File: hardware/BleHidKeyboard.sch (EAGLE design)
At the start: 13 parts, among them IC1 MCP23018SO, IC2 MCP23018SO, J1 BATTERY, J4 KEYBOARD_2X13, U1 DYNASTREAM_N5150M5CD

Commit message: Version 1 of PCB layout
This is the version that I sent to OSHPark to have manufactured on
3/14/2018.
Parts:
- removed J2: (no value), SparkFun-Connectors:M041X04_NO_SILK
- removed J3: (no value), SparkFun-Connectors:M01NOSILK-KIT
- added JP1: DEBUG, adam_custom:FTSH-105
- added JP2: FTDI, adafruit:PINHD-1X6CLEAN
- IC1, IC2: value MCP23018SO -> MCP23018SSOP; device adam_custom:MCP23018SO -> adam_custom:MCP23018SSOP
- renumbered LED1 to LED_NUM, LED2 to LED_CAPS, LED3 to LED_CONNECT
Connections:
- removed net INT: J3.1, U1.P3
- new net !RST/!SWDIO: JP1.2, U1.!RST!/SWDIO
- new net SWDCLK: JP1.4, U1.SWDCLK
- new net UART_RXD: JP2.4, U1.P12
- new net UART_TXD: JP2.5, U1.P6
- net GND: now also JP1.3, JP1.5, JP1.9, JP2.1, JP2.2
- net INTA-1: now also U1.P3; no longer J2.1
- net INTA-2: now also U1.P11; no longer J2.3
- net INTB-1: now also U1.P8; no longer J2.2
- net INTB-2: now also U1.P21; no longer J2.4
- net KEY1: now also IC1.GPB7; no longer IC1.GPA0
- net KEY10: now also IC1.GPA6; no longer IC1.GPB1
- net KEY11: now also IC1.GPA5; no longer IC1.GPB2
- net KEY12: now also IC1.GPA4; no longer IC1.GPB3
- net KEY13: now also IC1.GPA3; no longer IC1.GPB4
- net KEY14: now also IC1.GPA2; no longer IC1.GPB5
- net KEY15: now also IC1.GPA1; no longer IC1.GPB6
- net KEY16: now also IC1.GPA0; no longer IC1.GPB7
- net KEY17: now also IC2.GPB1; no longer IC2.GPA0
- net KEY18: now also IC2.GPB0; no longer IC2.GPA1
- net KEY19: now also IC2.GPA7; no longer IC2.GPA2
- net KEY2: now also IC1.GPB6; no longer IC1.GPA1
- net KEY20: now also IC2.GPA6; no longer IC2.GPA3
- net KEY21: now also IC2.GPA5; no longer IC2.GPA4
- net KEY22: now also IC2.GPA4; no longer IC2.GPA5
- net KEY23: now also IC2.GPA3; no longer IC2.GPA6
- net KEY24: now also IC2.GPA2; no longer IC2.GPA7
- net KEY25: now also IC2.GPA1; no longer IC2.GPB0
- net KEY26: now also IC2.GPA0; no longer IC2.GPB1
- net KEY3: now also IC1.GPB5; no longer IC1.GPA2
- net KEY4: now also IC1.GPB4; no longer IC1.GPA3
- net KEY5: now also IC1.GPB3; no longer IC1.GPA4
- net KEY6: now also IC1.GPB2; no longer IC1.GPA5
- net KEY7: now also IC1.GPB1; no longer IC1.GPA6
- net KEY8: now also IC1.GPB0; no longer IC1.GPA7
- net KEY9: now also IC1.GPA7; no longer IC1.GPB0
- net LED_CAPS: now also U1.P0; no longer U1.P5
- net LED_CONNECT: now also U1.P9; no longer U1.P6
- net LED_NUM: now also U1.P24; no longer U1.P4
- net SCL: now also U1.P15; no longer U1.P1
- net SDA: now also U1.P5; no longer U1.P2
- net VCC: now also JP1.1
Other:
- moved on the sheet: IC1, IC2, U1

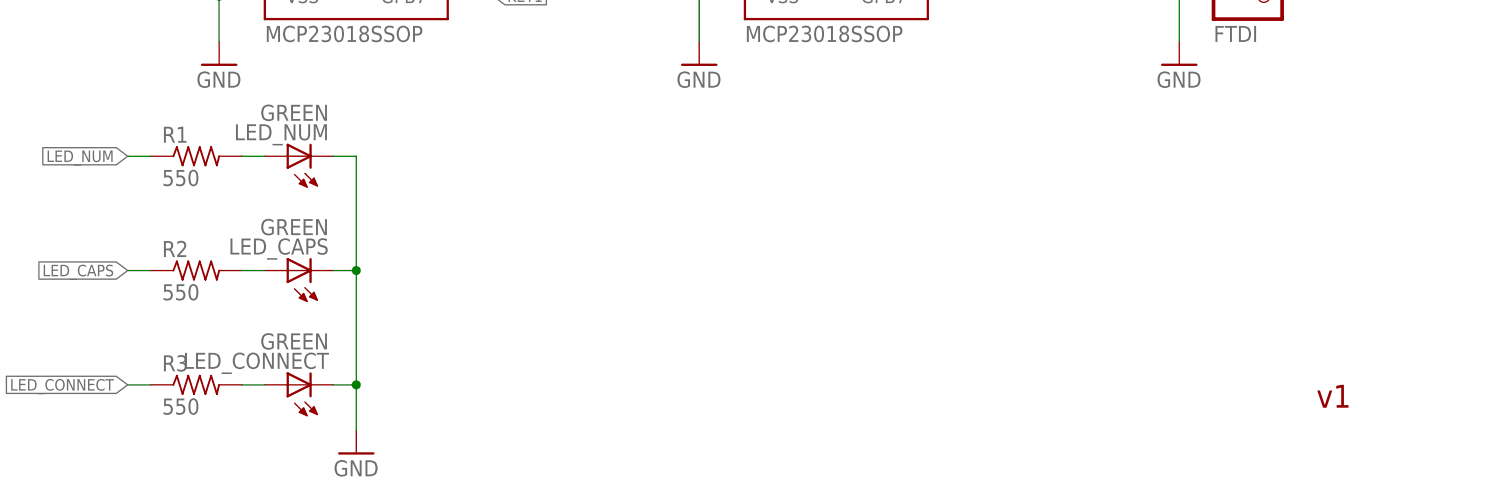
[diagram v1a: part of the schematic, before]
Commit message: Switch to 1.2k LED current limiting resistors
This reduces current usage by half but still leaves them bright enough
to see.
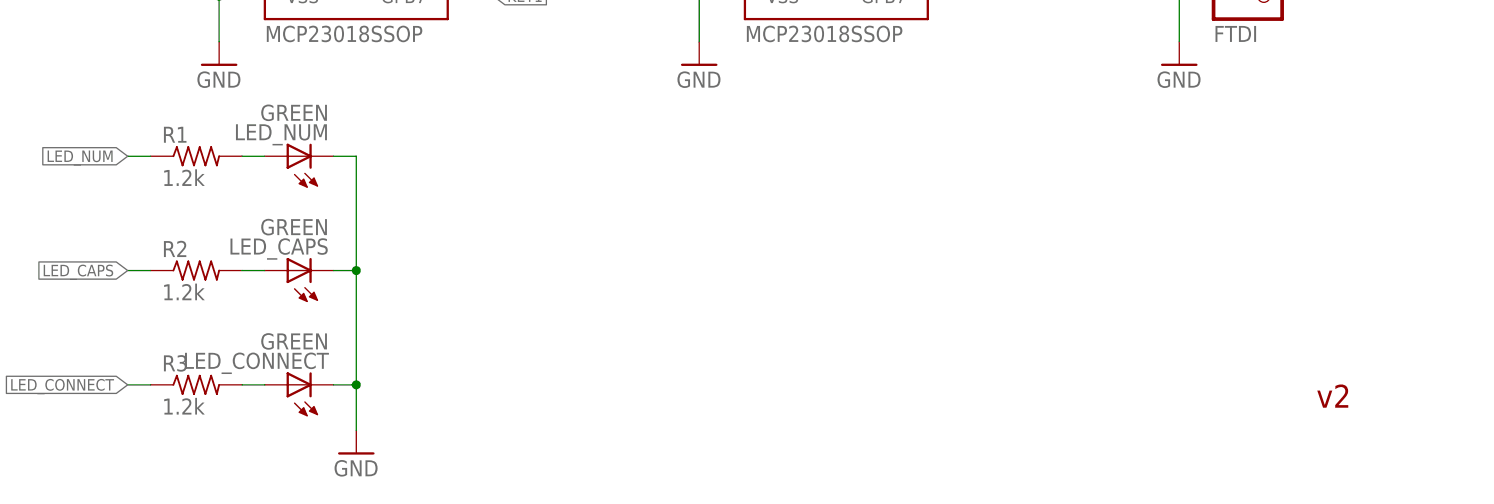
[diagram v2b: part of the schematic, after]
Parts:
- R1, R2, R3: value 550 -> 1.2k
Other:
- note added: "v2"
- note removed: "v1"
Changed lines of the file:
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@@
 <part name="GND4" library="SparkFun-Aesthetics" deviceset="GND" device=""/>
 <part name="J4" library="adam_custom" deviceset="KEYBOARD_2X13" device=""/>
-<part name="R1" library="rcl" deviceset="R-US_" device="R0805" value="550"/>
+<part name="R1" library="rcl" deviceset="R-US_" device="R0805" value="1.2k"/>
 <part name="LED_NUM" library="adafruit" deviceset="LED" device="CHIPLED_1206" value="GREEN"/>
-<part name="R2" library="rcl" deviceset="R-US_" device="R0805" value="550"/>
+<part name="R2" library="rcl" deviceset="R-US_" device="R0805" value="1.2k"/>
 <part name="LED_CAPS" library="adafruit" deviceset="LED" device="CHIPLED_1206" value="GREEN"/>
-<part name="R3" library="rcl" deviceset="R-US_" device="R0805" value="550"/>
+<part name="R3" library="rcl" deviceset="R-US_" device="R0805" value="1.2k"/>
 <part name="LED_CONNECT" library="adafruit" deviceset="LED" device="CHIPLED_1206" value="GREEN"/>
 <part name="GND5" library="SparkFun-Aesthetics" deviceset="GND" device=""/>
@@
 <sheet>
 <plain>
-<text x="233.68" y="10.16" size="2.54" layer="94">v1</text>
+<text x="233.68" y="10.16" size="2.54" layer="94">v2</text>
 </plain>
 <instances>

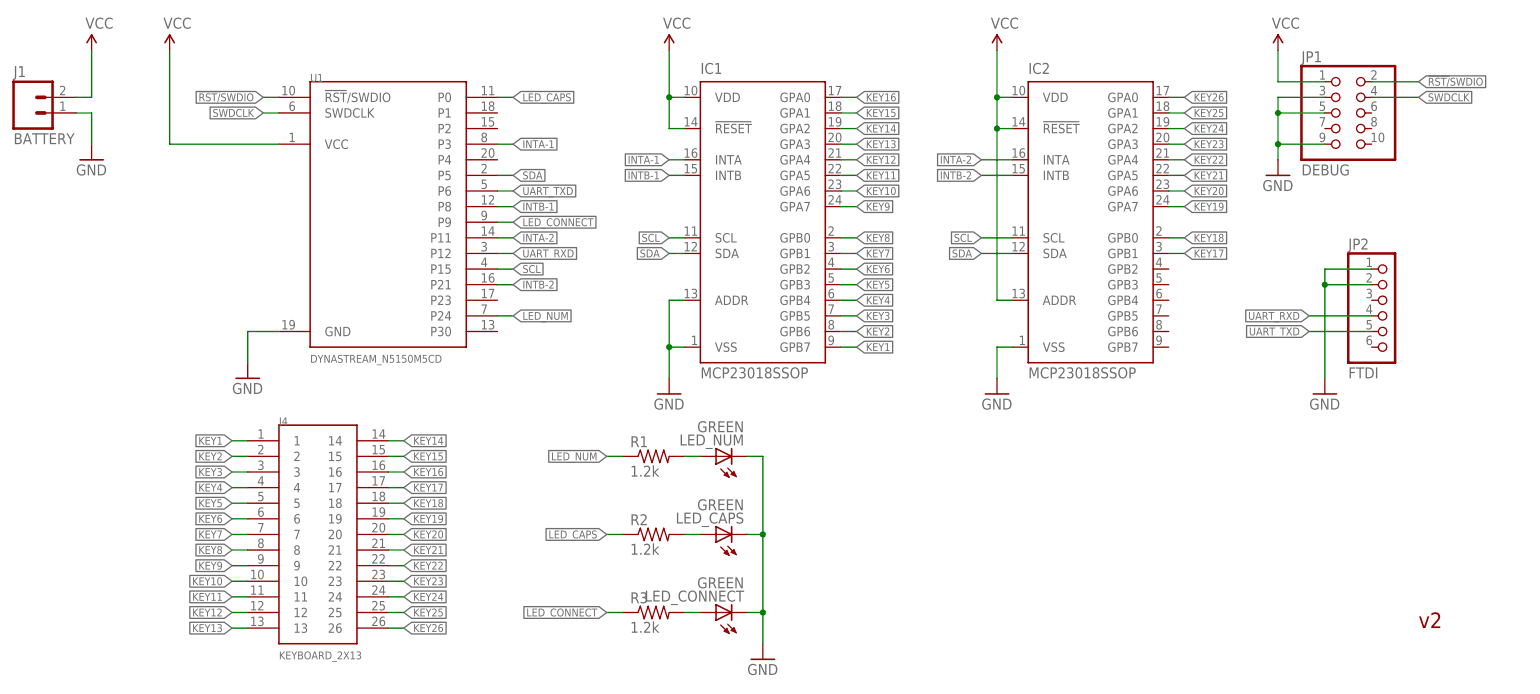
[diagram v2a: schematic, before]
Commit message: Version 3 of the PCB design
This is the design being sent off to OSHPark on May 6th, 2018.

This version of the PCB no longer uses the 20-pin Molex connector on
the bottom of the Dynastream N5150M5CD module and instead uses the
pads around the perimeter of the N5150M4CD module (actually the same
module but without the Molex and SWD connectors) instead. The module
will now mount on the bottom of the PCB with the module can sticking up
through a hole in this new PCB. This will give us extra height
clearance and correct the problem that the current PCB doesn't fit in
the original keyboard case.

I updated the firmware to accomodate the change in pin mappings for
UART, I2C, LEDs, etc.
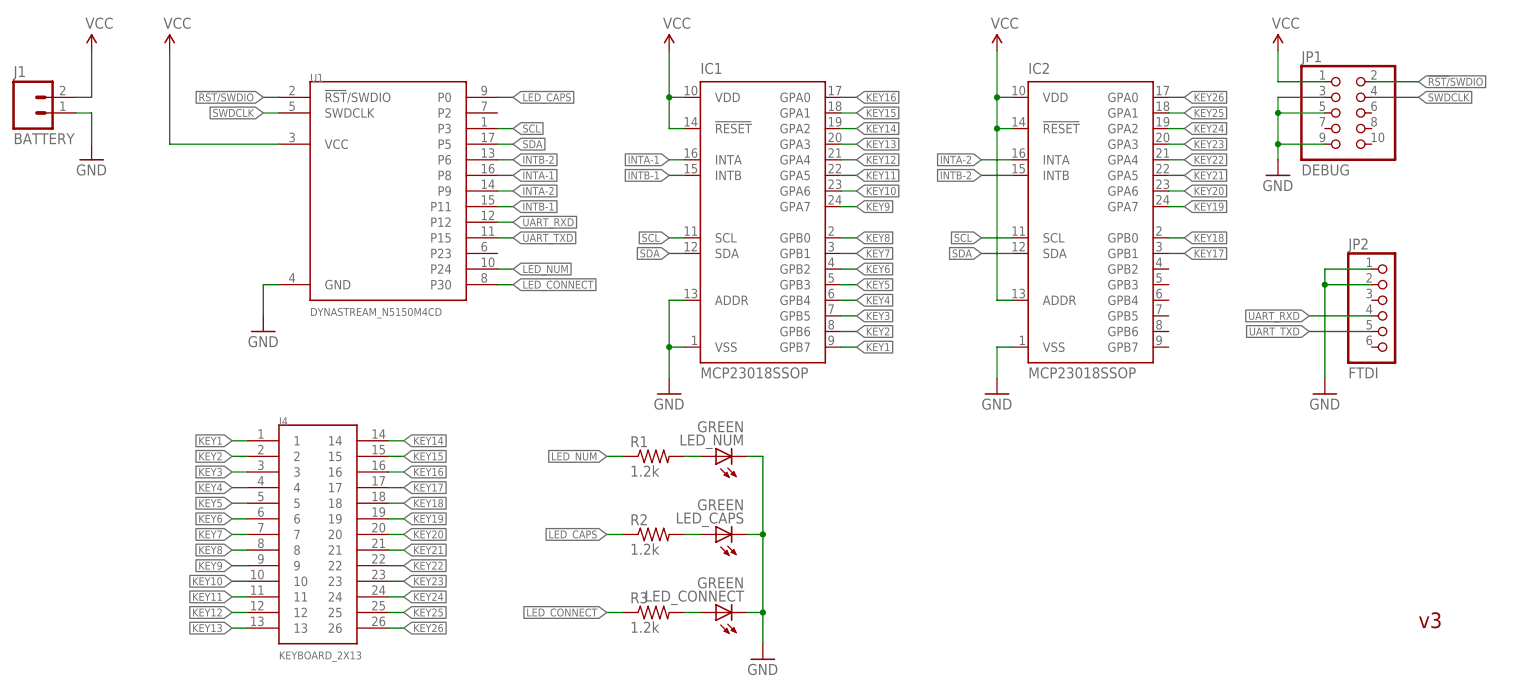
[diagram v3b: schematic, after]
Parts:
- U1: value DYNASTREAM_N5150M5CD -> DYNASTREAM_N5150M4CD; device adam_custom:DYNASTREAM_N5150M5CD -> adam_custom:DYNASTREAM_N5150M4CD
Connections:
- net INTA-1: now also U1.P8; no longer U1.P3
- net INTA-2: now also U1.P9; no longer U1.P11
- net INTB-1: now also U1.P11; no longer U1.P8
- net INTB-2: now also U1.P6; no longer U1.P21
- net LED_CONNECT: now also U1.P30; no longer U1.P9
- net SCL: now also U1.P3; no longer U1.P15
- net UART_TXD: now also U1.P15; no longer U1.P6
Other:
- note added: "v3"
- note removed: "v2"
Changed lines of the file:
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@@
 <part name="SUPPLY1" library="SparkFun-Aesthetics" deviceset="VCC" device=""/>
 <part name="GND1" library="SparkFun-Aesthetics" deviceset="GND" device=""/>
-<part name="U1" library="adam_custom" deviceset="DYNASTREAM_N5150M5CD" device=""/>
+<part name="U1" library="adam_custom" deviceset="DYNASTREAM_N5150M4CD" device=""/>
 <part name="SUPPLY2" library="SparkFun-Aesthetics" deviceset="VCC" device=""/>
 <part name="GND2" library="SparkFun-Aesthetics" deviceset="GND" device=""/>
@@
 <sheet>
 <plain>
-<text x="233.68" y="10.16" size="2.54" layer="94">v2</text>
+<text x="233.68" y="10.16" size="2.54" layer="94">v3</text>
 </plain>
 <instances>
@@
 <instance part="U1" gate="G$1" x="66.04" y="78.74"/>
 <instance part="SUPPLY2" gate="G$1" x="30.48" y="104.14"/>
-<instance part="GND2" gate="1" x="43.18" y="50.8"/>
+<instance part="GND2" gate="1" x="45.72" y="58.42"/>
 <instance part="IC1" gate="G$1" x="127" y="76.2"/>
 <instance part="SUPPLY3" gate="G$1" x="111.76" y="104.14"/>
@@
 </segment>
 <segment>
-<pinref part="U1" gate="G$1" pin="GND"/>
-<pinref part="GND2" gate="1" pin="GND"/>
-<wire x1="48.26" y1="58.42" x2="43.18" y2="58.42" width="0.1524" layer="91"/>
-<wire x1="43.18" y1="58.42" x2="43.18" y2="53.34" width="0.1524" layer="91"/>
-</segment>
-<segment>
 <pinref part="IC1" gate="G$1" pin="VSS"/>
 <pinref part="GND3" gate="1" pin="GND"/>
@@
 <junction x="218.44" y="66.04"/>
 </segment>
+<segment>
+<pinref part="U1" gate="G$1" pin="GND"/>
+<pinref part="GND2" gate="1" pin="GND"/>
+<wire x1="48.26" y1="66.04" x2="45.72" y2="66.04" width="0.1524" layer="91"/>
+<wire x1="45.72" y1="66.04" x2="45.72" y2="60.96" width="0.1524" layer="91"/>
+</segment>
 </net>
 <net name="SCL" class="0">
@@
 </segment>
 <segment>
-<pinref part="U1" gate="G$1" pin="P15"/>
-<wire x1="83.82" y1="68.58" x2="86.36" y2="68.58" width="0.1524" layer="91"/>
-<label x="86.36" y="68.58" size="1.27" layer="95" xref="yes"/>
+<pinref part="U1" gate="G$1" pin="P3"/>
+<wire x1="83.82" y1="91.44" x2="86.36" y2="91.44" width="0.1524" layer="91"/>
+<label x="86.36" y="91.44" size="1.27" layer="95" xref="yes"/>
 </segment>
 </net>
@@
 <segment>
 <pinref part="U1" gate="G$1" pin="P5"/>
-<wire x1="83.82" y1="83.82" x2="86.36" y2="83.82" width="0.1524" layer="91"/>
-<label x="86.36" y="83.82" size="1.27" layer="95" xref="yes"/>
+<wire x1="83.82" y1="88.9" x2="86.36" y2="88.9" width="0.1524" layer="91"/>
+<label x="86.36" y="88.9" size="1.27" layer="95" xref="yes"/>
 </segment>
 </net>
@@
 </segment>
 <segment>
-<pinref part="U1" gate="G$1" pin="P3"/>
-<wire x1="83.82" y1="88.9" x2="86.36" y2="88.9" width="0.1524" layer="91"/>
-<label x="86.36" y="88.9" size="1.27" layer="95" xref="yes"/>
+<pinref part="U1" gate="G$1" pin="P8"/>
+<wire x1="83.82" y1="83.82" x2="86.36" y2="83.82" width="0.1524" layer="91"/>
+<label x="86.36" y="83.82" size="1.27" layer="95" xref="yes"/>
 </segment>
 </net>
@@
 </segment>
 <segment>
-<pinref part="U1" gate="G$1" pin="P8"/>
+<pinref part="U1" gate="G$1" pin="P11"/>
 <wire x1="83.82" y1="78.74" x2="86.36" y2="78.74" width="0.1524" layer="91"/>
 <label x="86.36" y="78.74" size="1.27" layer="95" xref="yes"/>
@@
 </segment>
 <segment>
-<pinref part="U1" gate="G$1" pin="P11"/>
-<wire x1="83.82" y1="73.66" x2="86.36" y2="73.66" width="0.1524" layer="91"/>
-<label x="86.36" y="73.66" size="1.27" layer="95" xref="yes"/>
+<pinref part="U1" gate="G$1" pin="P9"/>
+<wire x1="83.82" y1="81.28" x2="86.36" y2="81.28" width="0.1524" layer="91"/>
+<label x="86.36" y="81.28" size="1.27" layer="95" xref="yes"/>
 </segment>
 </net>
@@
 </segment>
 <segment>
-<pinref part="U1" gate="G$1" pin="P21"/>
-<wire x1="83.82" y1="66.04" x2="86.36" y2="66.04" width="0.1524" layer="91"/>
-<label x="86.36" y="66.04" size="1.27" layer="95" xref="yes"/>
+<pinref part="U1" gate="G$1" pin="P6"/>
+<wire x1="83.82" y1="86.36" x2="86.36" y2="86.36" width="0.1524" layer="91"/>
+<label x="86.36" y="86.36" size="1.27" layer="95" xref="yes"/>
 </segment>
 </net>
@@
 <segment>
 <pinref part="U1" gate="G$1" pin="P24"/>
-<wire x1="83.82" y1="60.96" x2="86.36" y2="60.96" width="0.1524" layer="91"/>
-<label x="86.36" y="60.96" size="1.27" layer="95" xref="yes"/>
+<wire x1="83.82" y1="68.58" x2="86.36" y2="68.58" width="0.1524" layer="91"/>
+<label x="86.36" y="68.58" size="1.27" layer="95" xref="yes"/>
 </segment>
 </net>
@@
 </segment>
 <segment>
-<pinref part="U1" gate="G$1" pin="P9"/>
-<wire x1="83.82" y1="76.2" x2="86.36" y2="76.2" width="0.1524" layer="91"/>
-<label x="86.36" y="76.2" size="1.27" layer="95" xref="yes"/>
+<pinref part="U1" gate="G$1" pin="P30"/>
+<wire x1="83.82" y1="66.04" x2="86.36" y2="66.04" width="0.1524" layer="91"/>
+<label x="86.36" y="66.04" size="1.27" layer="95" xref="yes"/>
 </segment>
 </net>
@@
 </segment>
 <segment>
-<pinref part="U1" gate="G$1" pin="P6"/>
-<wire x1="83.82" y1="81.28" x2="86.36" y2="81.28" width="0.1524" layer="91"/>
-<label x="86.36" y="81.28" size="1.27" layer="95" xref="yes"/>
+<pinref part="U1" gate="G$1" pin="P15"/>
+<wire x1="83.82" y1="73.66" x2="86.36" y2="73.66" width="0.1524" layer="91"/>
+<label x="86.36" y="73.66" size="1.27" layer="95" xref="yes"/>
 </segment>
 </net>
@@
 <segment>
 <pinref part="U1" gate="G$1" pin="P12"/>
-<wire x1="83.82" y1="71.12" x2="86.36" y2="71.12" width="0.1524" layer="91"/>
-<label x="86.36" y="71.12" size="1.27" layer="95" xref="yes"/>
-</segment>
-</net>
+<wire x1="83.82" y1="76.2" x2="86.36" y2="76.2" width="0.1524" layer="91"/>
+<label x="86.36" y="76.2" size="1.27" layer="95" xref="yes"/>
+</segment>
+</net>
